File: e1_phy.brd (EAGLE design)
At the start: 100 x 75 mm, 127 parts, among them IC2 LD117AS33TR, IC3 LD117AS33TR, U1 IDT82V2081, U2 GPS_GNS_2201, U3 VCTCXO-CONNORWINFIELD, U4 VCXO_TAITIEN_VT, U5 IP4234CZ6, U7 IP4234CZ6, X2 SMA-142-0701-801/806, X3 JACK2.5_SJ-2523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

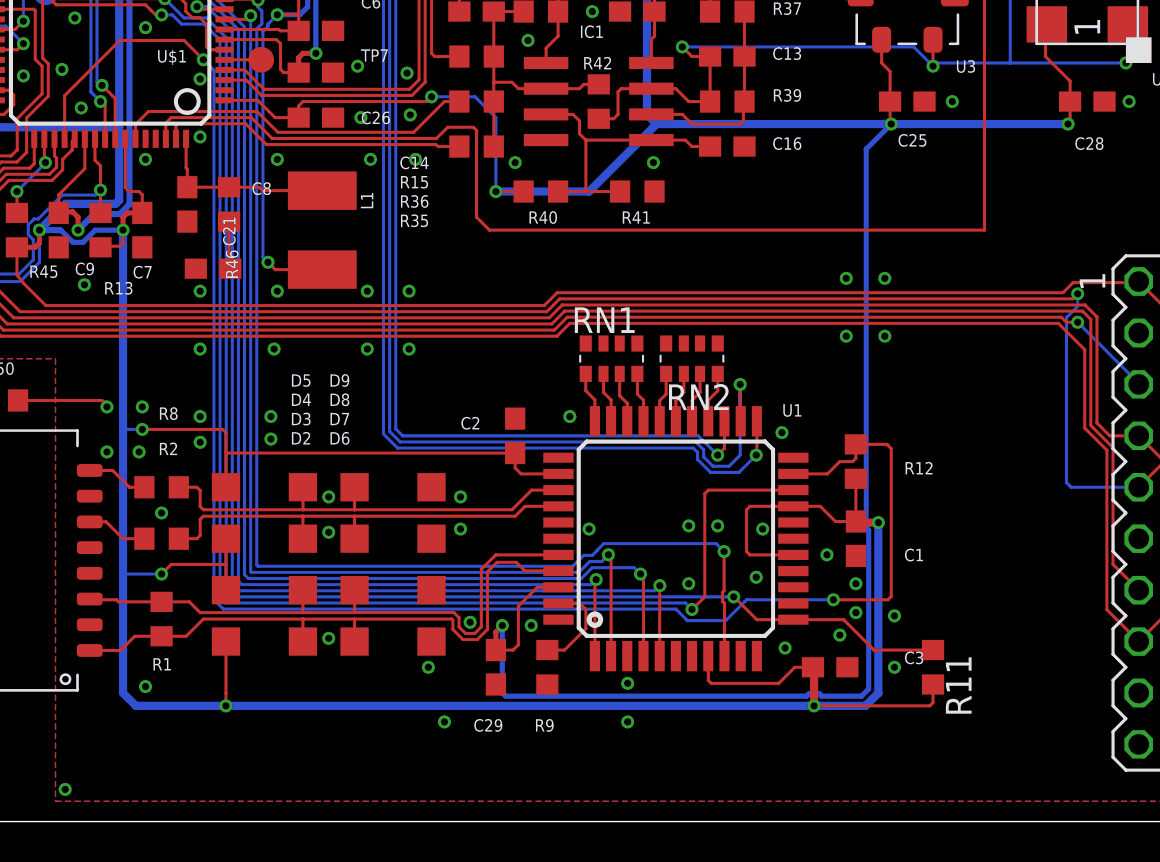
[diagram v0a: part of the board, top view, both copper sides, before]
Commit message: Moved LIU VDD_analog from +UB to Vcc+Inductor
(this is suggested in the datasheet, and I don't want to
 pollute the +UB (clean supply for oscillators))
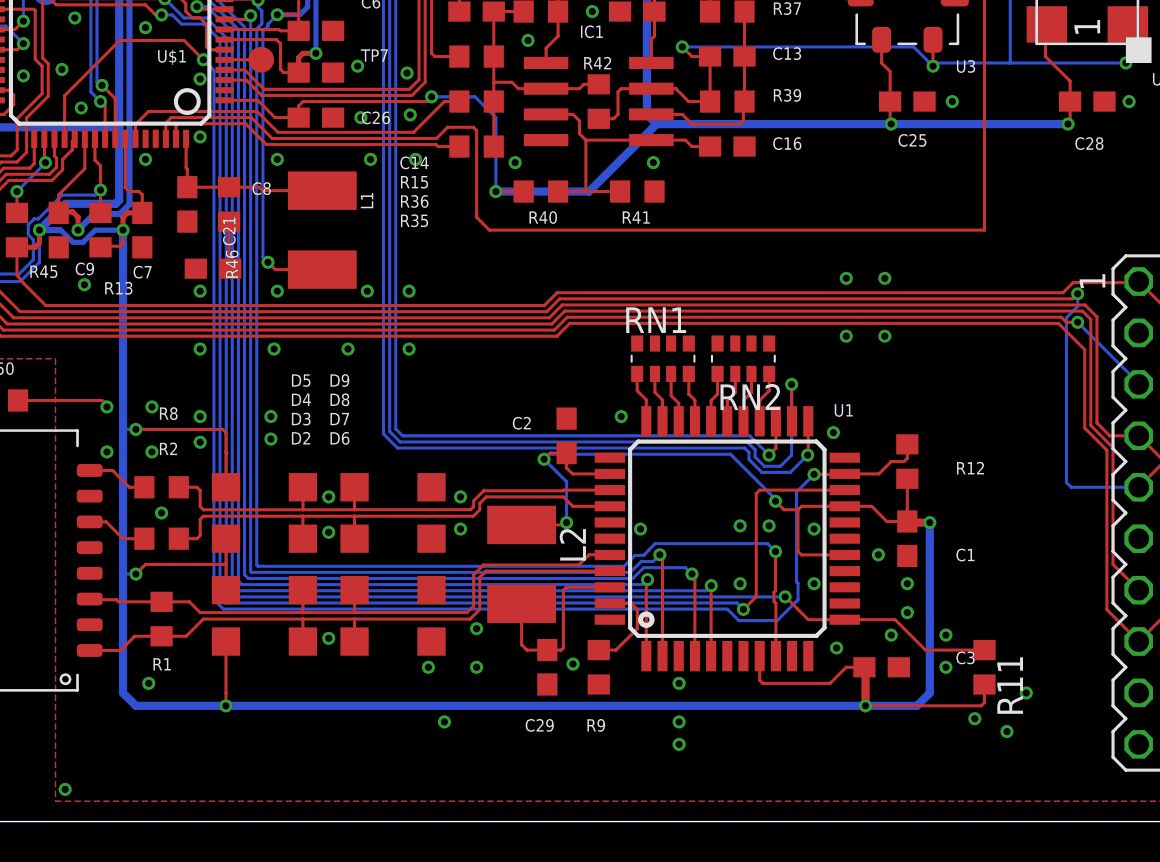
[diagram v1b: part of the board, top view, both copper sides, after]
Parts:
- added L2: 10uH, rcl:L1812
- moved C1 2.54 mm to (76.2, 14.0)
- moved C3 2.54 mm to (74.9, 7.62)
- moved R11 2.54 mm to (80.0, 7.62)
- moved R12 2.54 mm to (76.2, 17.8)
- moved RN1 2.54 mm to (64.1, 22.9)
- moved RN2 2.54 mm to (68.1, 22.9)
- moved U1 2.54 mm to (67.3, 14.0)
- moved C2 2.54 mm to (59.4, 19.1)
- moved C29 2.54 mm to (58.4, 7.62)
- moved R9 2.54 mm to (61.0, 7.62)
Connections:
- new net LIU_VDDA: C29.1, L2.2, U1.42
- net +UB: no longer C29.1, U1.42
- net VCC: now also L2.1
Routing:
- net +UB: track 203.1 -> 146.0 mm, vias 10 -> 9
- net LIU_VDDA: track 0.00 -> 9.44 mm
- net VCC: track 424.1 -> 433.5 mm, vias 12 -> 15
- net #SPI_CS1: track 85.0 -> 79.3 mm
- net TTIP: track 22.1 -> 25.2 mm
- net TRING: track 22.3 -> 25.0 mm
- net TX_CLK: track 62.1 -> 64.6 mm
- net SPI_MOSI: track 86.0 -> 88.6 mm
- net SPI_MISO: track 80.0 -> 82.6 mm
- net TX_DATA: track 52.0 -> 54.5 mm
- net RX_DATA: track 56.4 -> 58.9 mm
- net SPI_SCK: track 77.0 -> 79.6 mm
- net RX_CLK: track 56.8 -> 59.3 mm
- net CLK2048: track 58.8 -> 61.3 mm
- net #RST_LIU: track 77.3 -> 79.8 mm
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
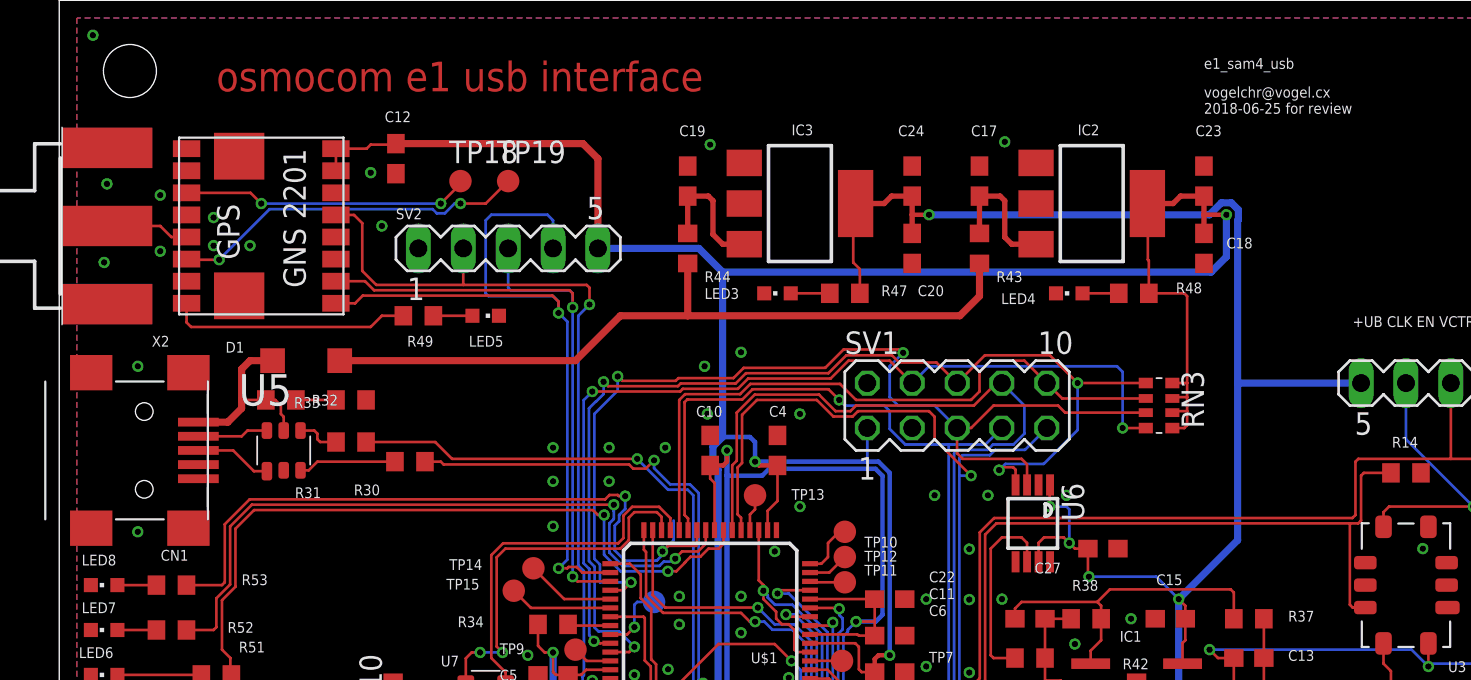
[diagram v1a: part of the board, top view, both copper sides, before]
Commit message: Review comments: Add ESD protection on GPS antenna.
0603ESDA-TR from laforge library.
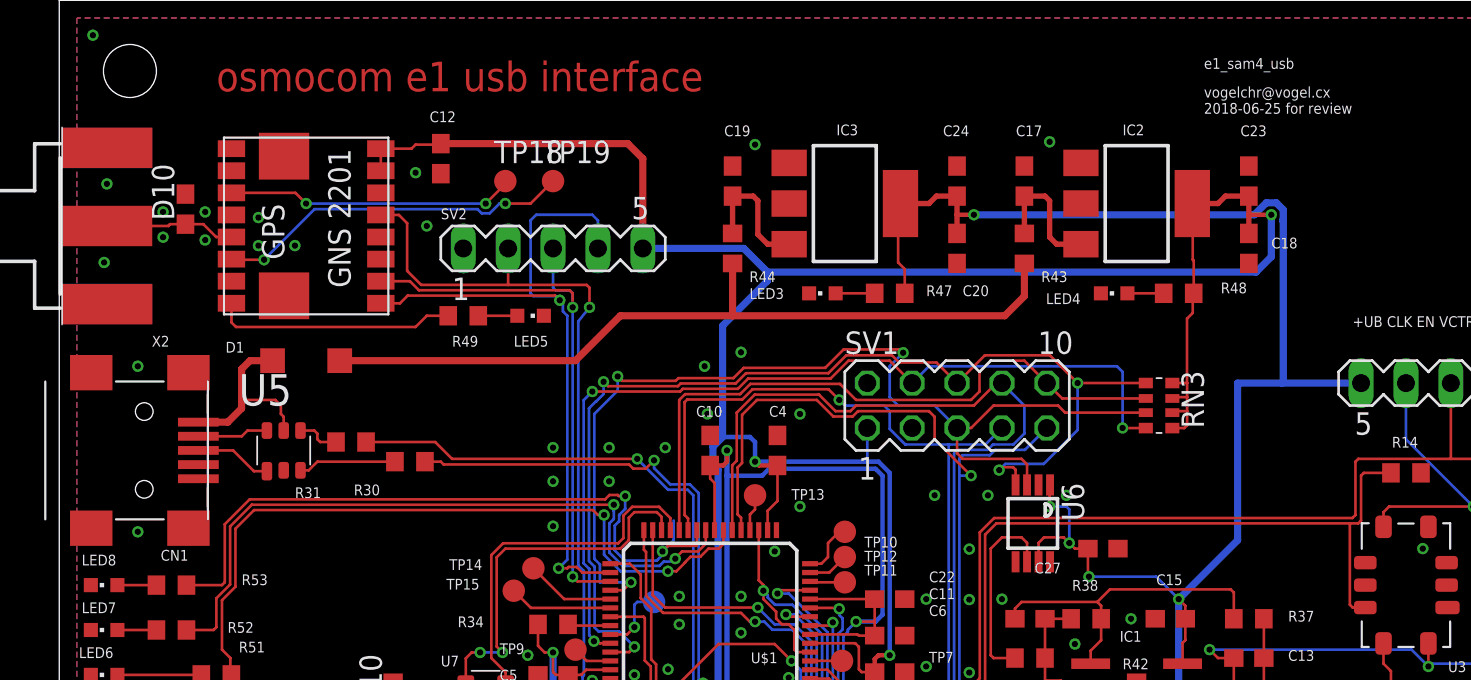
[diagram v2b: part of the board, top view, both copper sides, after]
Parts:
- removed R32: 27k, rcl:R0603
- removed R33: 47k, rcl:R0603
- added D10: 0603ESDA-TR, laforge:0603
- moved C18 2.54 mm to (67.3, 61.0)
- moved C23 2.54 mm to (67.3, 64.8)
- moved IC3 2.54 mm to (44.5, 63.5)
- moved LED5 2.54 mm to (26.7, 57.1)
- moved SV2 2.54 mm to (27.9, 61.0)
- moved TP19 2.54 mm to (27.9, 64.8)
- moved U2 2.54 mm to (14.0, 62.2)
- moved C12 2.54 mm to (21.6, 66.0)
- moved C17 2.54 mm to (54.6, 64.8)
- moved C19 2.54 mm to (38.1, 64.8)
- moved C20 2.54 mm to (50.8, 61.0)
- moved C24 2.54 mm to (50.8, 64.8)
- moved IC2 2.54 mm to (61.0, 63.5)
- moved LED3 2.54 mm to (43.2, 58.4)
- moved LED4 2.54 mm to (59.7, 58.4)
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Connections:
- removed net USB_VBUS_SENS: R32.1, R33.2
- net GND: now also D10.2; no longer R33.1
- net N$4: now also D10.1
- net VBUS_CONN: no longer R32.2
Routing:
- net GPS_SAM4_TX: track 46.3 -> 40.6 mm
- net GPS_SAM4_RX: track 38.8 -> 33.7 mm
- net N$4: track 4.74 -> 7.36 mm
- net GPS_PPS: track 44.9 -> 42.4 mm
- net USB_VBUS: track 42.5 -> 45.1 mm
- net USB_VBUS_SENS: track 2.27 -> 0.00 mm
- net VCC: track 433.5 -> 432.7 mm
- net VBUS_CONN: track 11.3 -> 10.8 mm
- net GND: vias 124 -> 126

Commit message: Regenerated v7 eagle files, made .pdf for schematic.
 -> next release candidate 20180703
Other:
- board text added: "vogelchr@vogel.cx 2018-07-03 for review"
- board text removed: "vogelchr@vogel.cx 2018-06-25 for review"

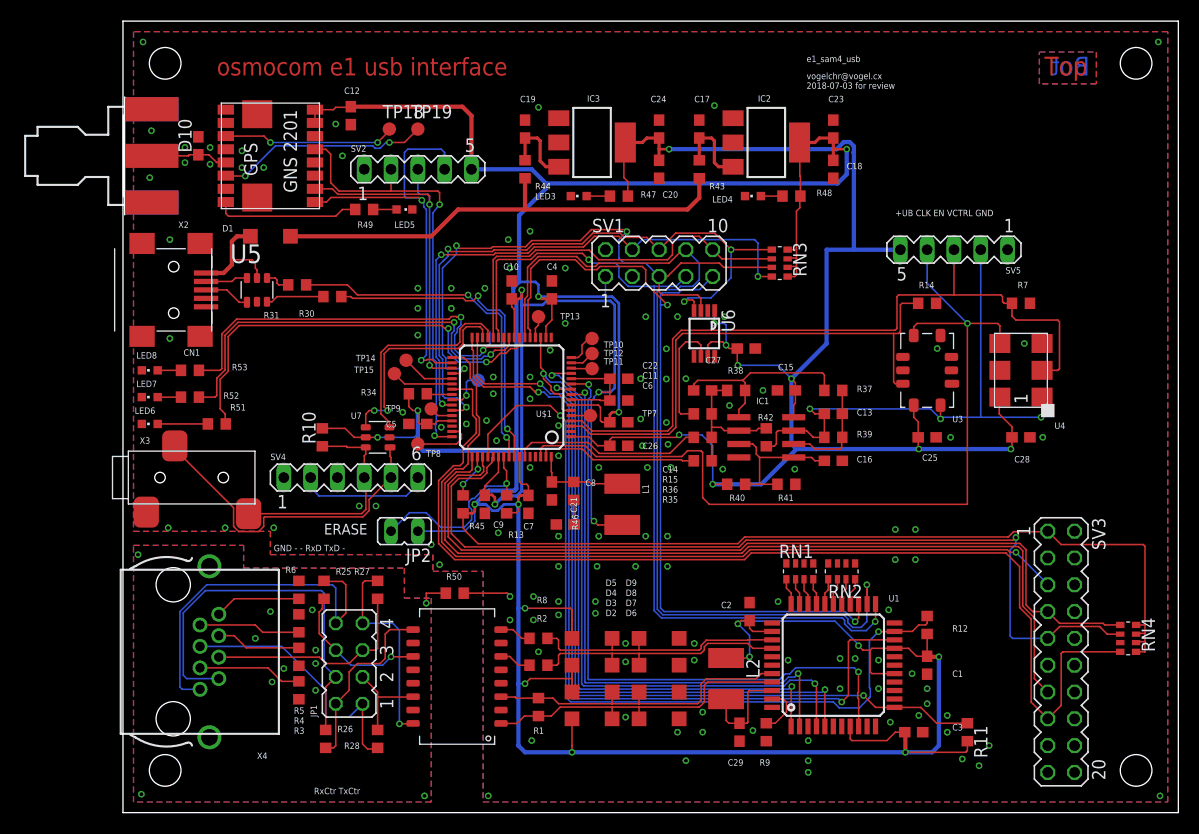
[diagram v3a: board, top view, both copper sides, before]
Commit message: 33R series resistor in clocks, RX/TX of PPS, SMA through hole
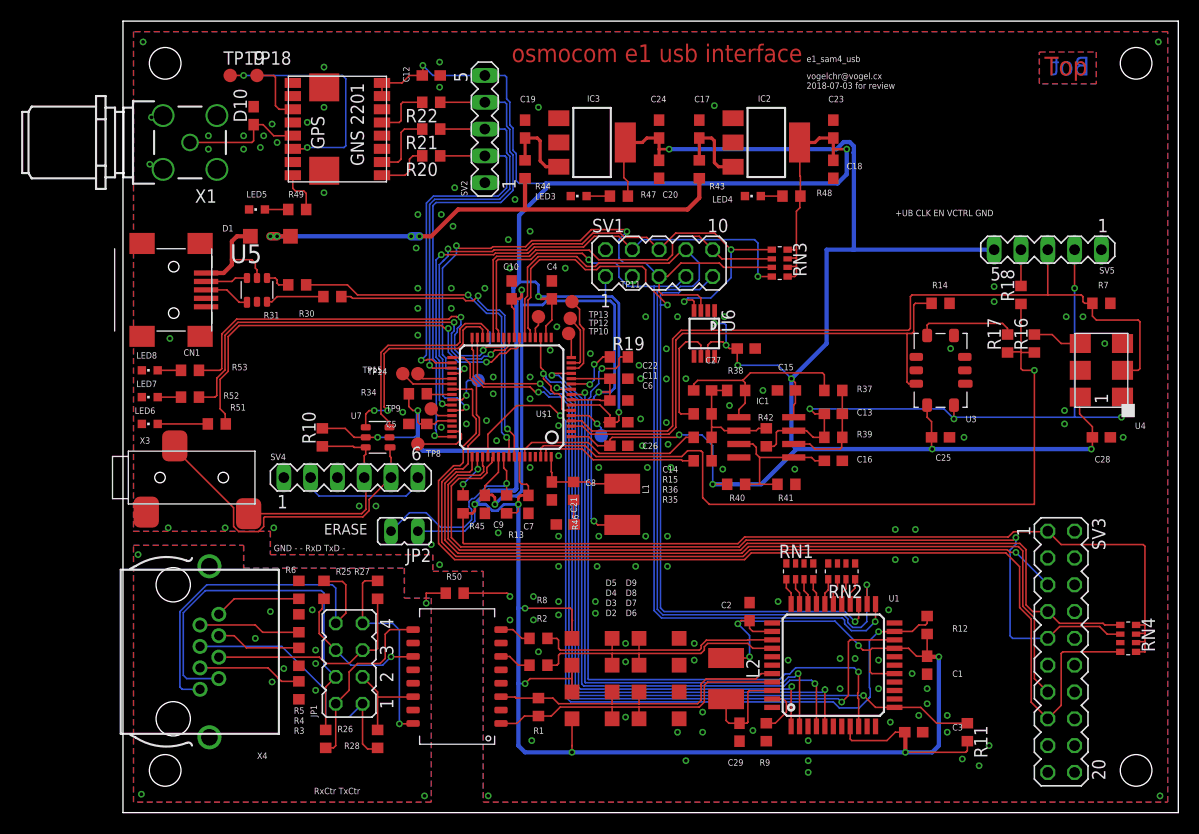
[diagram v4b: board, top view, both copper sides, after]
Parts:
- removed X2: SMA-142-0701-801/806, con-coax:J502-ND-142-0701-801/806
- added R16, R17, R18, R19, R20, R21, R22: 33R, rcl:R0603
- added X1: BU-SMA-G, con-coax:BU-SMA-G
- moved TP19 18.5 mm to (10.2, 69.8)
- moved LED5 14.0 mm to (12.7, 57.1), turned to 90 degrees
- moved TP18 13.5 mm to (12.7, 69.8)
- moved SV5 8.89 mm to (87.6, 53.3)
- moved C12 8.52 mm to (29.2, 69.8), turned to 0 degrees
- moved C28 7.62 mm to (92.7, 35.6)
- moved R7 7.62 mm to (92.7, 48.3)
- moved U4 7.62 mm to (92.7, 41.9)
- moved SV2 7.41 mm to (34.3, 64.8), turned to 90 degrees
- moved U2 6.84 mm to (20.3, 64.8)
- moved TP11 6.63 mm to (42.5, 48.4)
- moved R49 6.35 mm to (16.5, 57.1), turned to 0 degrees
- moved D10 5.97 mm to (12.4, 66.0)
- moved TP12 3.92 mm to (42.4, 46.8)
- moved TP10 2.27 mm to (42.2, 45.4)
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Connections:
- net N$10 renamed GPS_3DFIX
- net N$19 renamed TP12
- net N$20 renamed TP13
- net N$21 renamed TP7
- net N$22 renamed TP14
- net N$23 renamed TP15
- net N$24 renamed GPS_WAKEUP
- net N$6 renamed TP9
- net N$7 renamed TP8
- net N$8 renamed TP10
- net N$9 renamed TP11
- removed net N$4: D10.1, U2.5, X2.1
- new net CLK2048_SAM4S: R19.1, U$1.11
- new net GPS_RF: D10.1, U2.5, X1.1
- new net GPS_RX_A: R20.2, U2.9
- new net N$30: R22.2, U2.13
- new net SAM4S_CLK_EXT: R18.2, SV5.4
- new net SAM4S_CLK_VCTXO: R17.2, U3.5
- new net SAM4S_CLK_VCXO: R16.2, U4.4
- new net TPS_TX_A: R21.2, U2.10
- net CLK2048: now also R19.2; no longer U$1.11
- net GND: now also X1.2, X1.3, X1.4, X1.5; no longer X2.G@1, X2.G@2, X2.G@3, X2.G@4
- net GPS_PPS: now also R22.1, SV2.4; no longer SV2.2, U2.13
- net GPS_SAM4_RX: now also R21.1; no longer U2.10
- net GPS_SAM4_TX: now also R20.1, SV2.2; no longer SV2.4, U2.9
- net SAM4S_CLK: now also R16.1, R17.1, R18.1; no longer SV5.4, U3.5, U4.4
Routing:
- net +UB: track 146.1 -> 162.6 mm
- net GPS_RF: track 0.00 -> 11.8 mm
- net #GPS_RESET: track 16.4 -> 6.30 mm, vias 2 -> 0
- net GPS_3DFIX: track 13.7 -> 4.23 mm
- net SAM4S_CLK_VCTXO: track 0.00 -> 9.45 mm
- net VCXO_CTRL: track 52.3 -> 60.1 mm, vias 3 -> 4
- net VCXO_EN: track 71.1 -> 78.7 mm
- net SAM4S_CLK: track 83.2 -> 75.7 mm
- net N$4: track 7.36 -> 0.00 mm
- net TPS_TX_A: track 0.00 -> 6.60 mm
- net TP11: track 1.99 -> 7.71 mm
- net CLK2048_SAM4S: track 0.00 -> 5.64 mm, vias 0 -> 2
- net N$30: track 0.00 -> 5.54 mm
- net GPS_RX_A: track 0.00 -> 5.23 mm
- net GPS_SAM4_TX: track 40.6 -> 35.6 mm, vias 2 -> 1
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
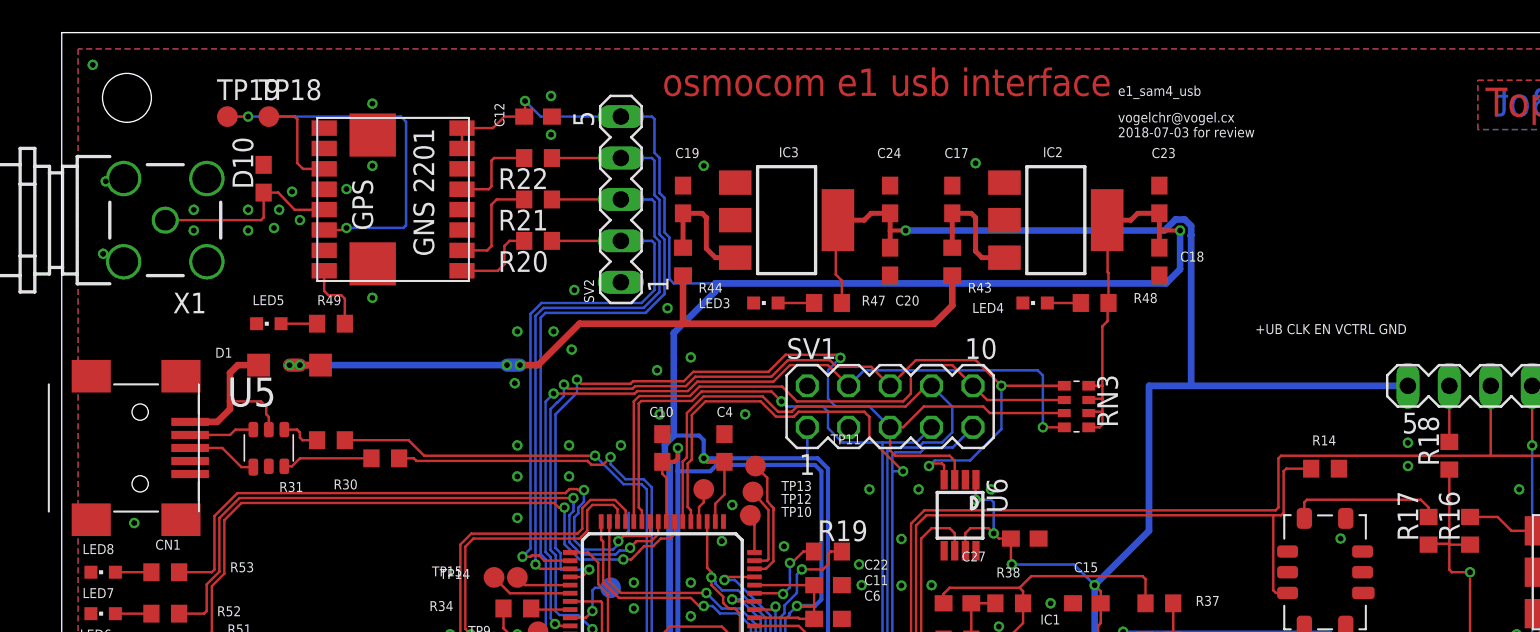
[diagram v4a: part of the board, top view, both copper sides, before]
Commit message: Add footprint for voltage reference, can be bypassed.
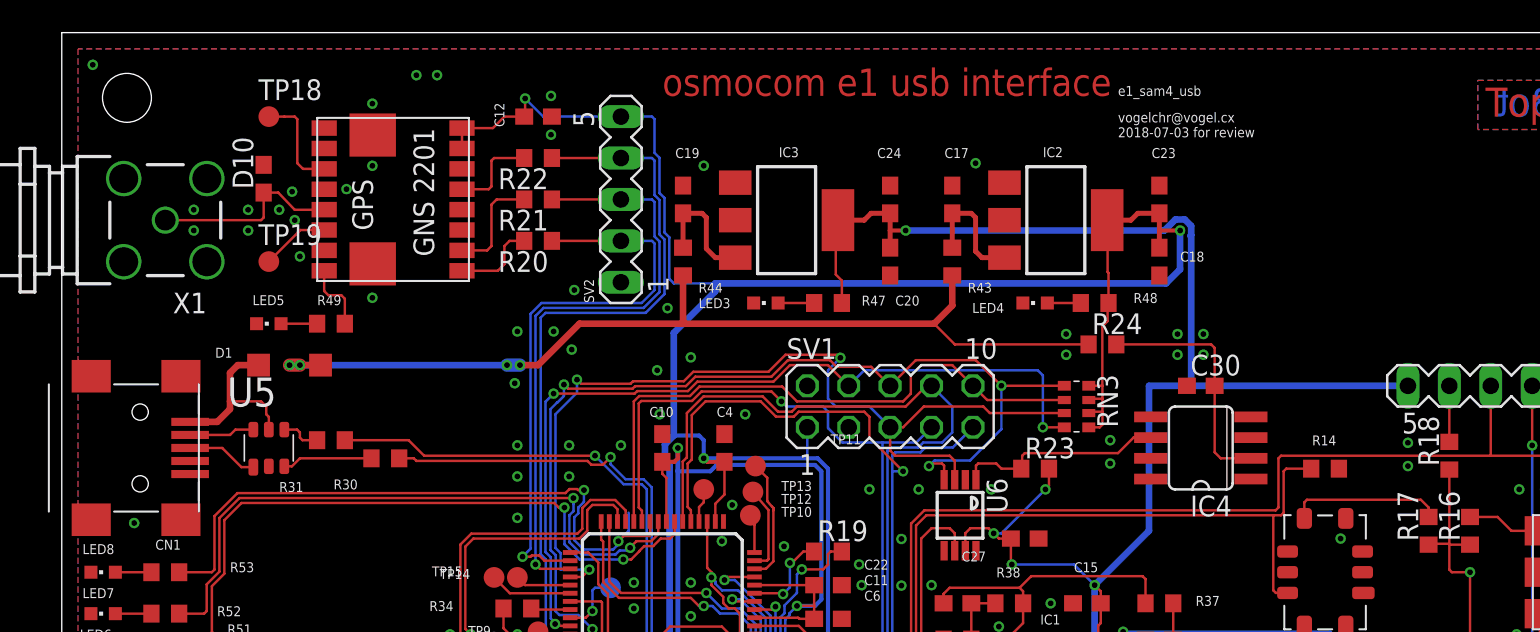
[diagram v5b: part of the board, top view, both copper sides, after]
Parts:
- added C30: 100n, rcl:C0603
- added IC4: MAX6173AASA, maxim:SO08
- added R23: 0R (DNP), rcl:R0603
- added R24: BLM/0R, rcl:R0603
- moved TP19 9.25 mm to (12.7, 61.0)
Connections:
- new net N$7: IC4.6, R23.1, U6.1
- new net N$9: C30.2, IC4.2, R24.2
- net +UB: now also R23.2; no longer U6.1
- net GND: now also C30.1, IC4.4
- net USB_VBUS: now also R24.1
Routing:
- net GPS_WAKEUP: track 22.8 -> 4.20 mm, vias 2 -> 0
- net N$9: track 0.00 -> 14.9 mm
- net N$7: track 0.00 -> 13.0 mm
- net USB_VBUS: track 48.2 -> 58.2 mm
- net +UB: track 162.6 -> 163.9 mm
- net GND: vias 144 -> 152
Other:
- board text removed: "+UB CLK EN VCTRL GND"
